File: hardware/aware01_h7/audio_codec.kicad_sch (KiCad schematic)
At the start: 6 parts, among them IC1 TLV320AIC3204IRHBR

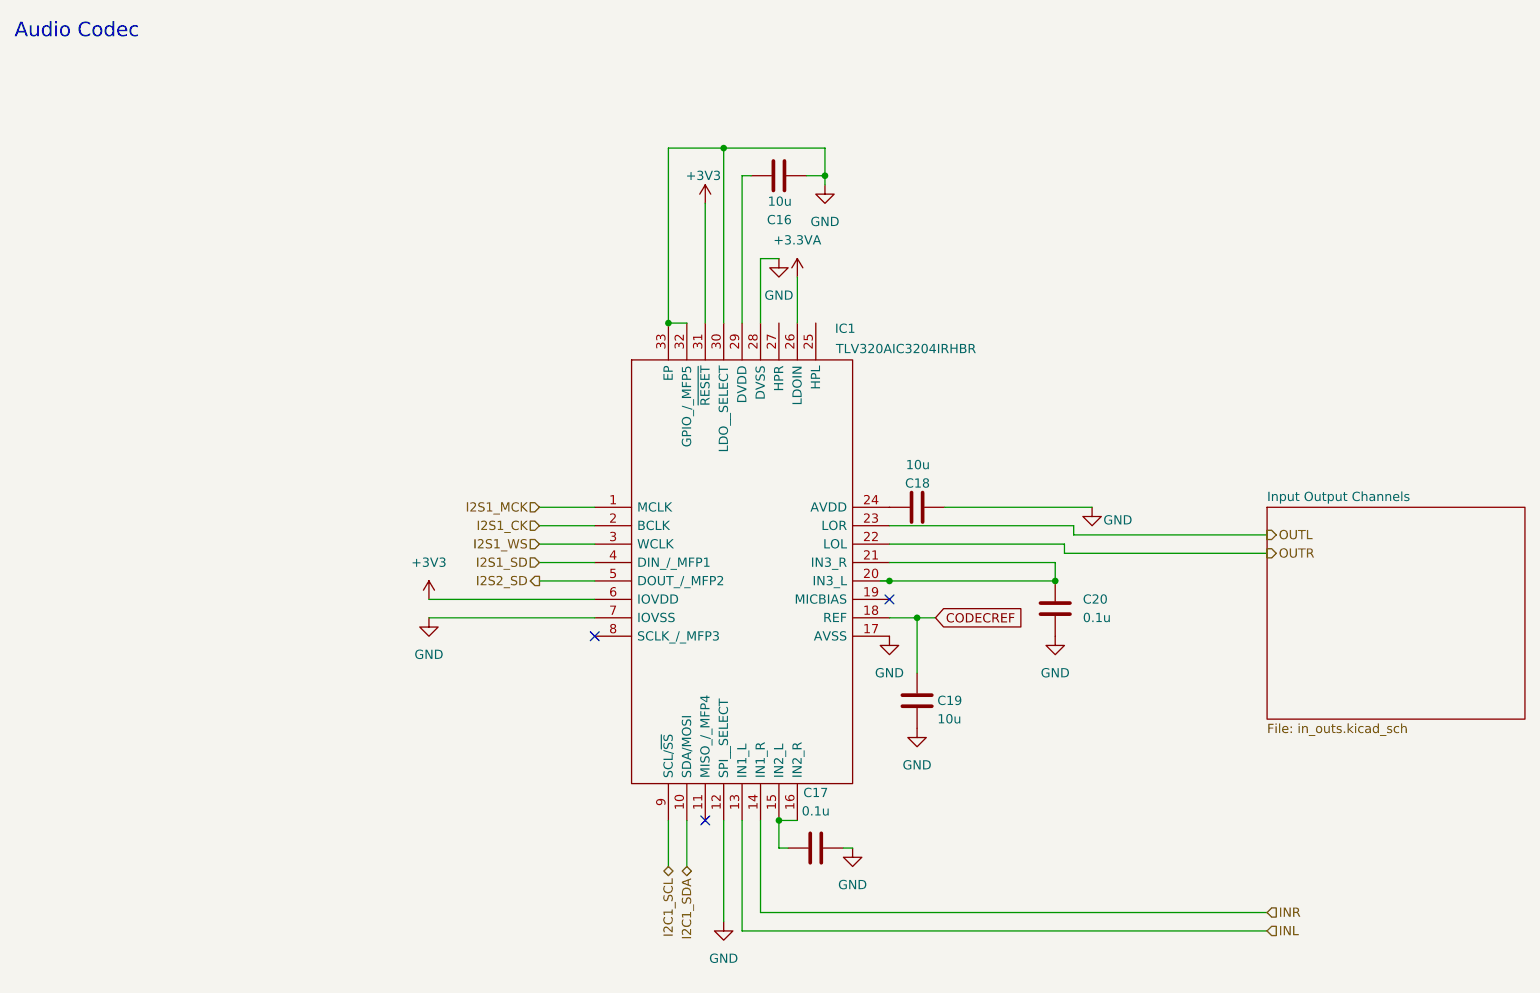
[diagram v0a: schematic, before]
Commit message: migrate to stm32h7 mcu
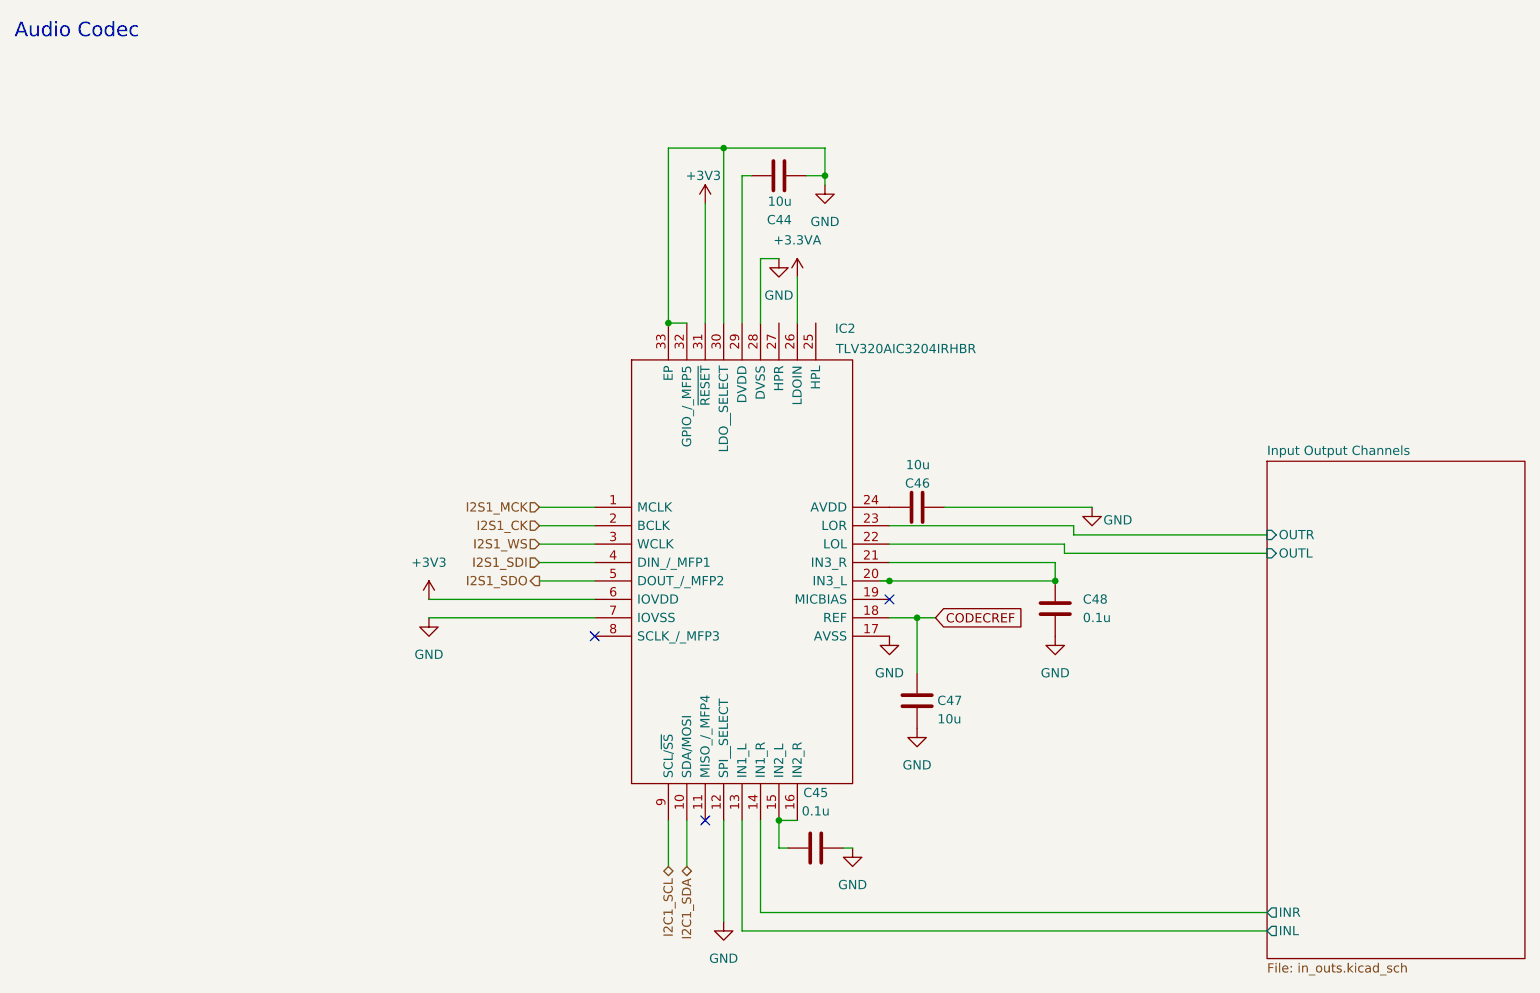
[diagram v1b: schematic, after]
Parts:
- renumbered C16 to C44, C17 to C45, C18 to C46, C19 to C47, C20 to C48, IC1 to IC2
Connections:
- net I2S1_SD renamed I2S1_SDI
- net I2S2_SD renamed I2S1_SDO
- net INL renamed Input Output Channels/INL
- net INR renamed Input Output Channels/INR
- net OUTL renamed Input Output Channels/OUTR
- net OUTR renamed Input Output Channels/OUTL
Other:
- sheet Input Output Channels ports: added INL, INR, OUTL, OUTR; removed none

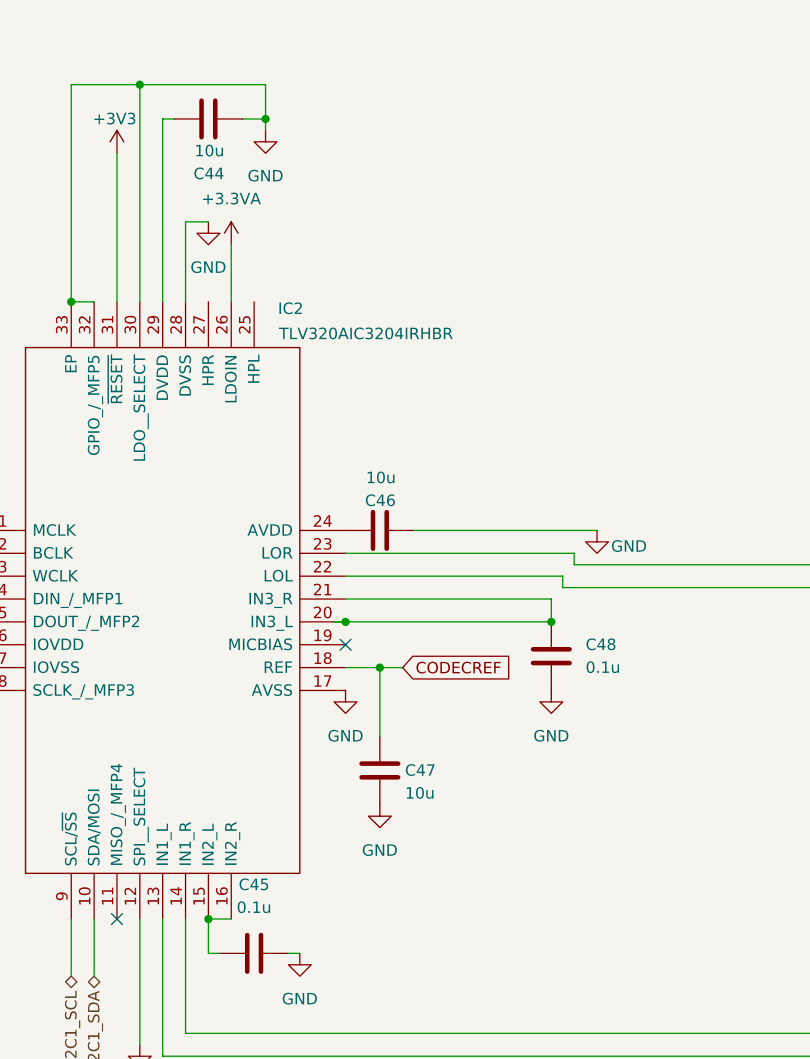
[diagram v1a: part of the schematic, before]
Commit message: update schematic
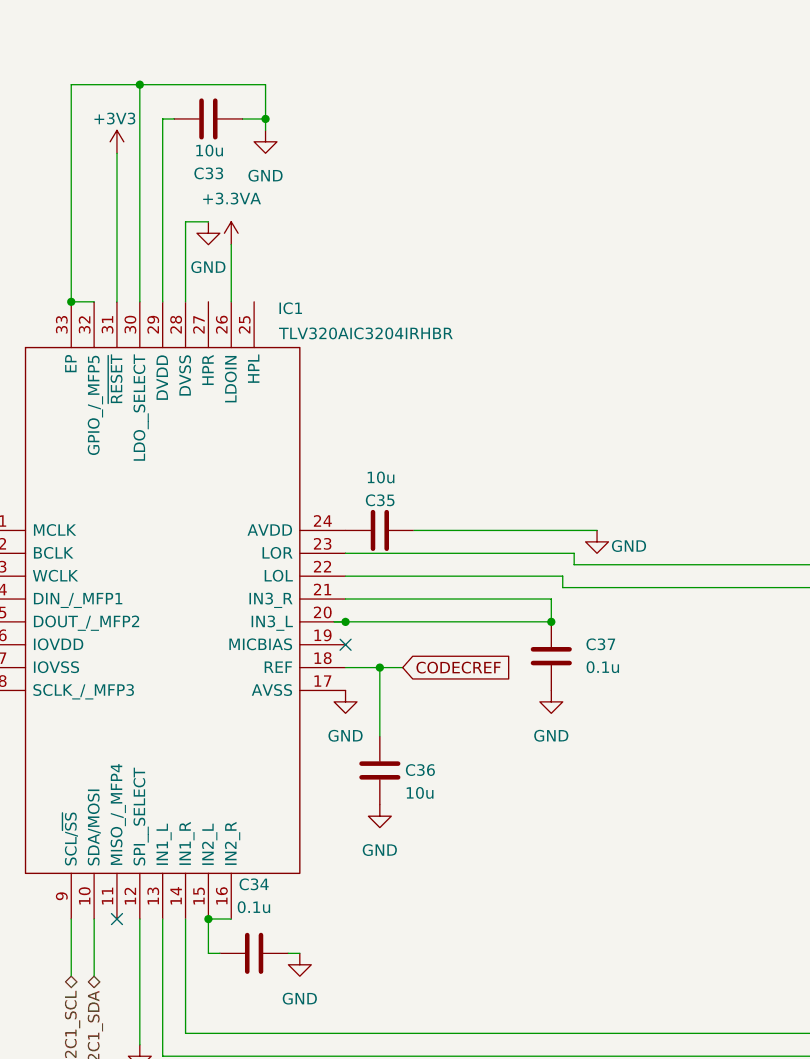
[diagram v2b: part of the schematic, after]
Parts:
- renumbered C44 to C33, C45 to C34, C46 to C35, C47 to C36, C48 to C37, IC2 to IC1
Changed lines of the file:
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@@
 		(on_board yes)
 		(dnp no)
-		(property "Reference" "#PWR087"
+		(property "Reference" "#PWR059"
 			(at 167.64 91.44 0)
 			(effects
@@
 			(project "ima_new_codec"
 				(path "/efd43d7c-3c18-45dd-8fa5-4bf32165850f/50dd69da-5058-483c-924f-252f04b072bd"
-					(reference "#PWR087")
+					(reference "#PWR059")
 					(unit 1)
 				)
@@
 		(on_board yes)
 		(dnp no)
-		(property "Reference" "#PWR078"
+		(property "Reference" "#PWR050"
 			(at 114.3 46.99 0)
 			(effects
@@
 			(project "ima_new_codec"
 				(path "/efd43d7c-3c18-45dd-8fa5-4bf32165850f/50dd69da-5058-483c-924f-252f04b072bd"
-					(reference "#PWR078")
+					(reference "#PWR050")
 					(unit 1)
 				)
@@
 		(dnp no)
 		(fields_autoplaced yes)
-		(property "Reference" "#PWR083"
+		(property "Reference" "#PWR055"
 			(at 134.62 138.43 0)
 			(effects
@@
 			(project "ima_new_codec"
 				(path "/efd43d7c-3c18-45dd-8fa5-4bf32165850f/50dd69da-5058-483c-924f-252f04b072bd"
-					(reference "#PWR083")
+					(reference "#PWR055")
 					(unit 1)
 				)
@@
 		(on_board yes)
 		(dnp no)
-		(property "Reference" "C47"
+		(property "Reference" "C36"
 			(at 146.304 111.76 0)
 			(effects
@@
 			(project "ima_new_codec"
 				(path "/efd43d7c-3c18-45dd-8fa5-4bf32165850f/50dd69da-5058-483c-924f-252f04b072bd"
-					(reference "C47")
+					(reference "C36")
 					(unit 1)
 				)
@@
 		(on_board yes)
 		(dnp no)
-		(property "Reference" "C44"
+		(property "Reference" "C33"
 			(at 126.238 45.466 90)
 			(effects
@@
 			(project "ima_new_codec"
 				(path "/efd43d7c-3c18-45dd-8fa5-4bf32165850f/50dd69da-5058-483c-924f-252f04b072bd"
-					(reference "C44")
+					(reference "C33")
 					(unit 1)
 				)
@@
 		(on_board yes)
 		(dnp no)
-		(property "Reference" "C46"
+		(property "Reference" "C35"
 			(at 145.288 81.788 90)
 			(effects
@@
 			(project "ima_new_codec"
 				(path "/efd43d7c-3c18-45dd-8fa5-4bf32165850f/50dd69da-5058-483c-924f-252f04b072bd"
-					(reference "C46")
+					(reference "C35")
 					(unit 1)
 				)
@@
 		(dnp no)
 		(fields_autoplaced yes)
-		(property "Reference" "#PWR080"
+		(property "Reference" "#PWR052"
 			(at 124.46 57.15 0)
 			(effects
@@
 			(project "ima_new_codec"
 				(path "/efd43d7c-3c18-45dd-8fa5-4bf32165850f/50dd69da-5058-483c-924f-252f04b072bd"
-					(reference "#PWR080")
+					(reference "#PWR052")
 					(unit 1)
 				)
@@
 		(dnp no)
 		(fields_autoplaced yes)
-		(property "Reference" "#PWR086"
+		(property "Reference" "#PWR058"
 			(at 162.56 109.22 0)
 			(effects
@@
 			(project "ima_new_codec"
 				(path "/efd43d7c-3c18-45dd-8fa5-4bf32165850f/50dd69da-5058-483c-924f-252f04b072bd"
-					(reference "#PWR086")
+					(reference "#PWR058")
 					(unit 1)
 				)
@@
 		(dnp no)
 		(fields_autoplaced yes)
-		(property "Reference" "C48"
+		(property "Reference" "C37"
 			(at 166.37 97.7899 0)
 			(effects
@@
 			(project "ima_new_codec"
 				(path "/efd43d7c-3c18-45dd-8fa5-4bf32165850f/50dd69da-5058-483c-924f-252f04b072bd"
-					(reference "C48")
+					(reference "C37")
 					(unit 1)
 				)
@@
 		(dnp no)
 		(fields_autoplaced yes)
-		(property "Reference" "#PWR076"
+		(property "Reference" "#PWR048"
 			(at 76.2 101.6 0)
 			(effects
@@
 			(project "ima_new_codec"
 				(path "/efd43d7c-3c18-45dd-8fa5-4bf32165850f/50dd69da-5058-483c-924f-252f04b072bd"
-					(reference "#PWR076")
+					(reference "#PWR048")
 					(unit 1)
 				)
@@
 		(dnp no)
 		(fields_autoplaced yes)
-		(property "Reference" "#PWR082"
+		(property "Reference" "#PWR054"
 			(at 130.81 46.99 0)
 			(effects
@@
 			(project "ima_new_codec"
 				(path "/efd43d7c-3c18-45dd-8fa5-4bf32165850f/50dd69da-5058-483c-924f-252f04b072bd"
-					(reference "#PWR082")
+					(reference "#PWR054")
 					(unit 1)
 				)
@@
 		(dnp no)
 		(fields_autoplaced yes)
-		(property "Reference" "#PWR085"
+		(property "Reference" "#PWR057"
 			(at 143.51 121.92 0)
 			(effects
@@
 			(project "ima_new_codec"
 				(path "/efd43d7c-3c18-45dd-8fa5-4bf32165850f/50dd69da-5058-483c-924f-252f04b072bd"
-					(reference "#PWR085")
+					(reference "#PWR057")
 					(unit 1)
 				)
@@
 		(dnp no)
 		(fields_autoplaced yes)
-		(property "Reference" "#PWR077"
+		(property "Reference" "#PWR049"
 			(at 76.2 106.68 0)
 			(effects
@@
 			(project "ima_new_codec"
 				(path "/efd43d7c-3c18-45dd-8fa5-4bf32165850f/50dd69da-5058-483c-924f-252f04b072bd"
-					(reference "#PWR077")
+					(reference "#PWR049")
 					(unit 1)
 				)
@@
 		(dnp no)
 		(fields_autoplaced yes)
-		(property "Reference" "C45"
+		(property "Reference" "C34"
 			(at 129.54 124.46 90)
 			(effects
@@
 			(project "ima_new_codec"
 				(path "/efd43d7c-3c18-45dd-8fa5-4bf32165850f/50dd69da-5058-483c-924f-252f04b072bd"
-					(reference "C45")
+					(reference "C34")
 					(unit 1)
 				)
@@
 		(dnp no)
 		(fields_autoplaced yes)
-		(property "Reference" "#PWR084"
+		(property "Reference" "#PWR056"
 			(at 139.7 109.22 0)
 			(effects
@@
 			(project "ima_new_codec"
 				(path "/efd43d7c-3c18-45dd-8fa5-4bf32165850f/50dd69da-5058-483c-924f-252f04b072bd"
-					(reference "#PWR084")
+					(reference "#PWR056")
 					(unit 1)
 				)
@@
 		(on_board yes)
 		(dnp no)
-		(property "Reference" "IC2"
+		(property "Reference" "IC1"
 			(at 133.604 60.452 0)
 			(effects
@@
 			(project "ima_new_codec"
 				(path "/efd43d7c-3c18-45dd-8fa5-4bf32165850f/50dd69da-5058-483c-924f-252f04b072bd"
-					(reference "IC2")
+					(reference "IC1")
 					(unit 1)
 				)
@@
 		(dnp no)
 		(fields_autoplaced yes)
-		(property "Reference" "#PWR081"
+		(property "Reference" "#PWR053"
 			(at 127 57.15 0)
 			(effects
@@
 			(project "ima_new_codec"
 				(path "/efd43d7c-3c18-45dd-8fa5-4bf32165850f/50dd69da-5058-483c-924f-252f04b072bd"
-					(reference "#PWR081")
+					(reference "#PWR053")
 					(unit 1)
 				)
@@
 		(dnp no)
 		(fields_autoplaced yes)
-		(property "Reference" "#PWR079"
+		(property "Reference" "#PWR051"
 			(at 116.84 148.59 0)
 			(effects
@@
 			(project "ima_new_codec"
 				(path "/efd43d7c-3c18-45dd-8fa5-4bf32165850f/50dd69da-5058-483c-924f-252f04b072bd"
-					(reference "#PWR079")
-					(unit 1)
-				)
+					(reference "#PWR051")
+					(unit 1)
+				)

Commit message: refine schematic
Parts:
- C33, C35, C36: footprint (none) -> Capacitor_SMD:C_0603_1608Metric
- C34, C37: value 0.1u -> 100n; footprint (none) -> Capacitor_SMD:C_0603_1608Metric
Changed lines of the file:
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@@
+	)
+	(junction
+		(at 130.81 44.45)
+		(diameter 0)
+		(color 0 0 0 0)
 	)
 	(junction
@@
 	)
 	(junction
-		(at 139.7 95.25)
-		(diameter 0)
-		(color 0 0 0 0)
-	)
-	(junction
 		(at 116.84 35.56)
 		(diameter 0)
@@
 	(wire
 		(pts
+			(xy 128.27 44.45) (xy 130.81 44.45)
+		)
+		(stroke
+			(width 0)
+			(type default)
+		)
+	)
+	(wire
+		(pts
 			(xy 124.46 128.27) (xy 127 128.27)
 		)
@@
 	(wire
 		(pts
-			(xy 121.92 50.8) (xy 121.92 59.69)
+			(xy 121.92 48.26) (xy 121.92 59.69)
 		)
 		(stroke
@@
 	(wire
 		(pts
-			(xy 130.81 39.37) (xy 130.81 40.64)
+			(xy 130.81 44.45) (xy 130.81 49.53)
+		)
+		(stroke
+			(width 0)
+			(type default)
+		)
+	)
+	(wire
+		(pts
+			(xy 130.81 39.37) (xy 130.81 44.45)
 		)
 		(stroke
@@
 	(wire
 		(pts
-			(xy 124.46 50.8) (xy 121.92 50.8)
-		)
-		(stroke
-			(width 0)
-			(type default)
-		)
-	)
-	(wire
-		(pts
-			(xy 138.43 95.25) (xy 139.7 95.25)
+			(xy 127 54.61) (xy 127 59.69)
+		)
+		(stroke
+			(width 0)
+			(type default)
+		)
+	)
+	(wire
+		(pts
+			(xy 121.92 48.26) (xy 128.27 48.26)
 		)
 		(stroke
@@
 	(wire
 		(pts
-			(xy 127 53.34) (xy 127 59.69)
+			(xy 138.43 50.8) (xy 138.43 54.61)
 		)
 		(stroke
@@
 	(wire
 		(pts
+			(xy 128.27 48.26) (xy 128.27 44.45)
+		)
+		(stroke
+			(width 0)
+			(type default)
+		)
+	)
+	(wire
+		(pts
 			(xy 124.46 132.08) (xy 124.46 128.27)
 		)
@@
 		(pts
 			(xy 191.77 143.51) (xy 119.38 143.51)
+		)
+		(stroke
+			(width 0)
+			(type default)
+		)
+	)
+	(wire
+		(pts
+			(xy 138.43 54.61) (xy 127 54.61)
 		)
 		(stroke
@@
 					(size 1.27 1.27)
 				)
+				(hide yes)
 			)
 		)
@@
 					(size 1.27 1.27)
 				)
+				(hide yes)
 			)
 		)
@@
 			)
 		)
-		(property "Footprint" ""
+		(property "Footprint" "Capacitor_SMD:C_0603_1608Metric"
 			(at 142.5448 107.95 0)
 			(effects
@@
 			)
 		)
-		(property "Footprint" ""
+		(property "Footprint" "Capacitor_SMD:C_0603_1608Metric"
 			(at 120.65 40.3352 0)
 			(effects
@@
 			)
 		)
-		(property "Footprint" ""
+		(property "Footprint" "Capacitor_SMD:C_0603_1608Metric"
 			(at 139.7 86.0552 0)
 			(effects
@@
 				(path "/efd43d7c-3c18-45dd-8fa5-4bf32165850f/50dd69da-5058-483c-924f-252f04b072bd"
 					(reference "C35")
-					(unit 1)
-				)
-			)
-		)
-	)
-	(symbol
-		(lib_id "power:GND")
-		(at 124.46 50.8 0)
-		(unit 1)
-		(exclude_from_sim no)
-		(in_bom yes)
-		(on_board yes)
-		(dnp no)
-		(fields_autoplaced yes)
-		(property "Reference" "#PWR052"
-			(at 124.46 57.15 0)
-			(effects
-				(font
-					(size 1.27 1.27)
-				)
-				(hide yes)
-			)
-		)
-		(property "Value" "GND"
-			(at 124.46 55.88 0)
-			(effects
-				(font
-					(size 1.27 1.27)
-				)
-			)
-		)
-		(property "Footprint" ""
-			(at 124.46 50.8 0)
-			(effects
-				(font
-					(size 1.27 1.27)
-				)
-				(hide yes)
-			)
-		)
-		(property "Datasheet" ""
-			(at 124.46 50.8 0)
-			(effects
-				(font
-					(size 1.27 1.27)
-				)
-				(hide yes)
-			)
-		)
-		(property "Description" "Power symbol creates a global label with name \"GND\" , ground"
-			(at 124.46 50.8 0)
-			(effects
-				(font
-					(size 1.27 1.27)
-				)
-				(hide yes)
-			)
-		)
-		(pin "1"
-		)
-		(instances
-			(project "ima_new_codec"
-				(path "/efd43d7c-3c18-45dd-8fa5-4bf32165850f/50dd69da-5058-483c-924f-252f04b072bd"
-					(reference "#PWR052")
 					(unit 1)
 				)
@@
 					(size 1.27 1.27)
 				)
+				(hide yes)
 			)
 		)
@@
 			)
 		)
-		(property "Value" "0.1u"
+		(property "Value" "100n"
 			(at 166.37 100.3299 0)
 			(effects
@@
 			)
 		)
-		(property "Footprint" ""
+		(property "Footprint" "Capacitor_SMD:C_0603_1608Metric"
 			(at 161.5948 95.25 0)
 			(effects
@@
 	(symbol
 		(lib_id "power:GND")
-		(at 130.81 40.64 0)
+		(at 130.81 49.53 0)
 		(unit 1)
 		(exclude_from_sim no)
@@
 		(fields_autoplaced yes)
 		(property "Reference" "#PWR054"
-			(at 130.81 46.99 0)
+			(at 130.81 55.88 0)
 			(effects
 				(font
@@
 		)
 		(property "Value" "GND"
-			(at 130.81 45.72 0)
-			(effects
-				(font
-					(size 1.27 1.27)
-				)
+			(at 130.81 54.61 0)
+			(effects
+				(font
+					(size 1.27 1.27)
+				)
+				(hide yes)
 			)
 		)
 		(property "Footprint" ""
-			(at 130.81 40.64 0)
+			(at 130.81 49.53 0)
 			(effects
 				(font
@@
 		)
 		(property "Datasheet" ""
-			(at 130.81 40.64 0)
+			(at 130.81 49.53 0)
 			(effects
 				(font
@@
 		)
 		(property "Description" "Power symbol creates a global label with name \"GND\" , ground"
-			(at 130.81 40.64 0)
+			(at 130.81 49.53 0)
 			(effects
 				(font
@@
 					(size 1.27 1.27)
 				)
+				(hide yes)
 			)
 		)
@@
 					(size 1.27 1.27)
 				)
+				(hide yes)
 			)
 		)
@@
 			)
 		)
-		(property "Value" "0.1u"
+		(property "Value" "100n"
 			(at 129.54 127 90)
 			(effects
@@
 			)
 		)
-		(property "Footprint" ""
+		(property "Footprint" "Capacitor_SMD:C_0603_1608Metric"
 			(at 133.35 131.1148 0)
 			(effects
@@
 	(symbol
 		(lib_id "power:+3.3VA")
-		(at 127 53.34 0)
+		(at 138.43 50.8 0)
 		(unit 1)
 		(exclude_from_sim no)
@@
 		(fields_autoplaced yes)
 		(property "Reference" "#PWR053"
-			(at 127 57.15 0)
+			(at 138.43 54.61 0)
 			(effects
 				(font
@@
 		)
 		(property "Value" "+3.3VA"
-			(at 127 48.26 0)
+			(at 138.43 45.72 0)
 			(effects
 				(font
@@
 		)
 		(property "Footprint" ""
-			(at 127 53.34 0)
+			(at 138.43 50.8 0)
 			(effects
 				(font
@@
 		)
 		(property "Datasheet" ""
-			(at 127 53.34 0)
+			(at 138.43 50.8 0)
 			(effects
 				(font
@@
 		)
 		(property "Description" "Power symbol creates a global label with name \"+3.3VA\""
-			(at 127 53.34 0)
+			(at 138.43 50.8 0)
 			(effects
 				(font
@@
 					(size 1.27 1.27)
 				)
+				(hide yes)
 			)
 		)
@@
 	)
 	(sheet
-		(at 191.77 78.74)
-		(size 35.56 68.58)
+		(at 191.77 83.82)
+		(size 35.56 63.5)
 		(fields_autoplaced yes)
 		(stroke
@@
 		)
 		(property "Sheetname" "Input Output Channels"
-			(at 191.77 78.0284 0)
-			(effects
-				(font
+			(at 191.77 83.1084 0)
+			(effects
+				(font
